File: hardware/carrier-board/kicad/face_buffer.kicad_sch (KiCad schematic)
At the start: 0 parts

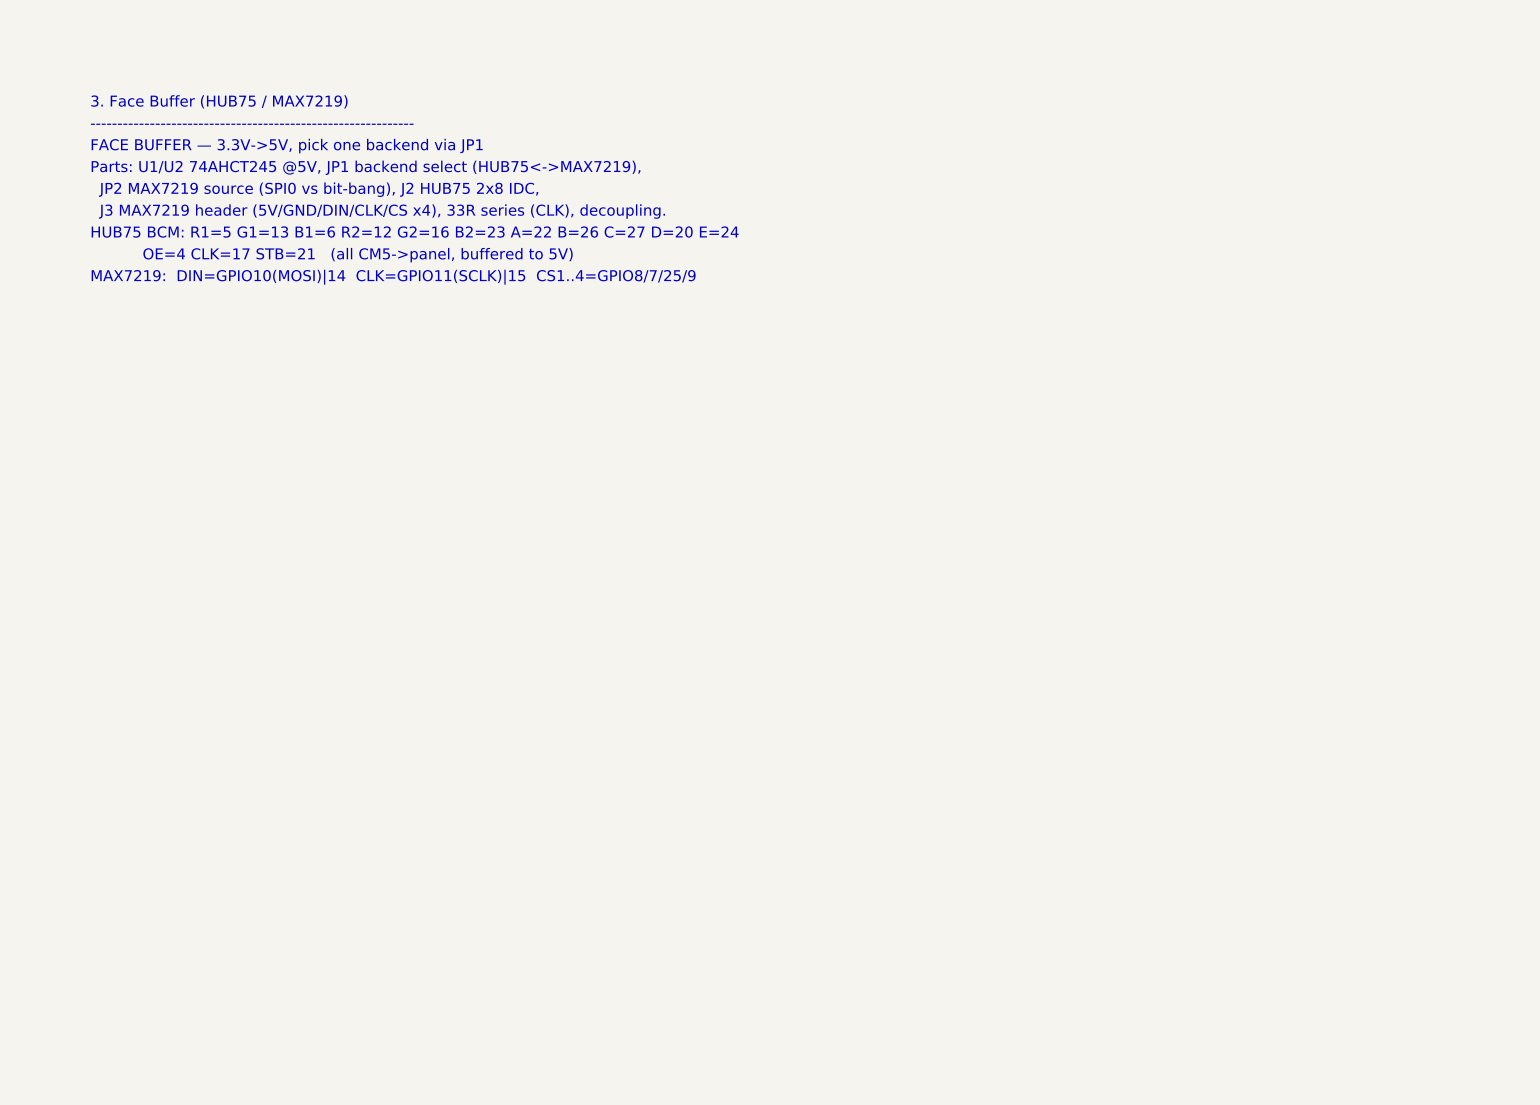
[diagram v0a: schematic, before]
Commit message: Carrier KiCad: populate face_buffer proof sheet (HUB75/MAX7219 '245 buffer)
Turn the face_buffer stub into a real, openable schematic as a format proof
before populating the remaining sheets:

- U1/U2 74AHCT245 @5V, DIR=+5V /OE=GND; R1-R3 33R series on CLK/LAT/OE;
  J2 HUB75 2x8 IDC, J3 MAX7219 1x8 header, JP2 DIN source select, C1/C2 decoupling.
- Netlist via labels placed on pin connection points (survives Update-from-Library):
  CM5-side GPIOxx as hierarchical labels per PINMAP kHub75 map, buffered
  R1/G1/.../E to J2, +5V/GND as global labels.
- KiCad 9 format (20250114), official lib_ids with embedded cached bodies.

Generated by populate_face_buffer.py (to be folded into generate_skeleton.py
once the format is validated in KiCad).
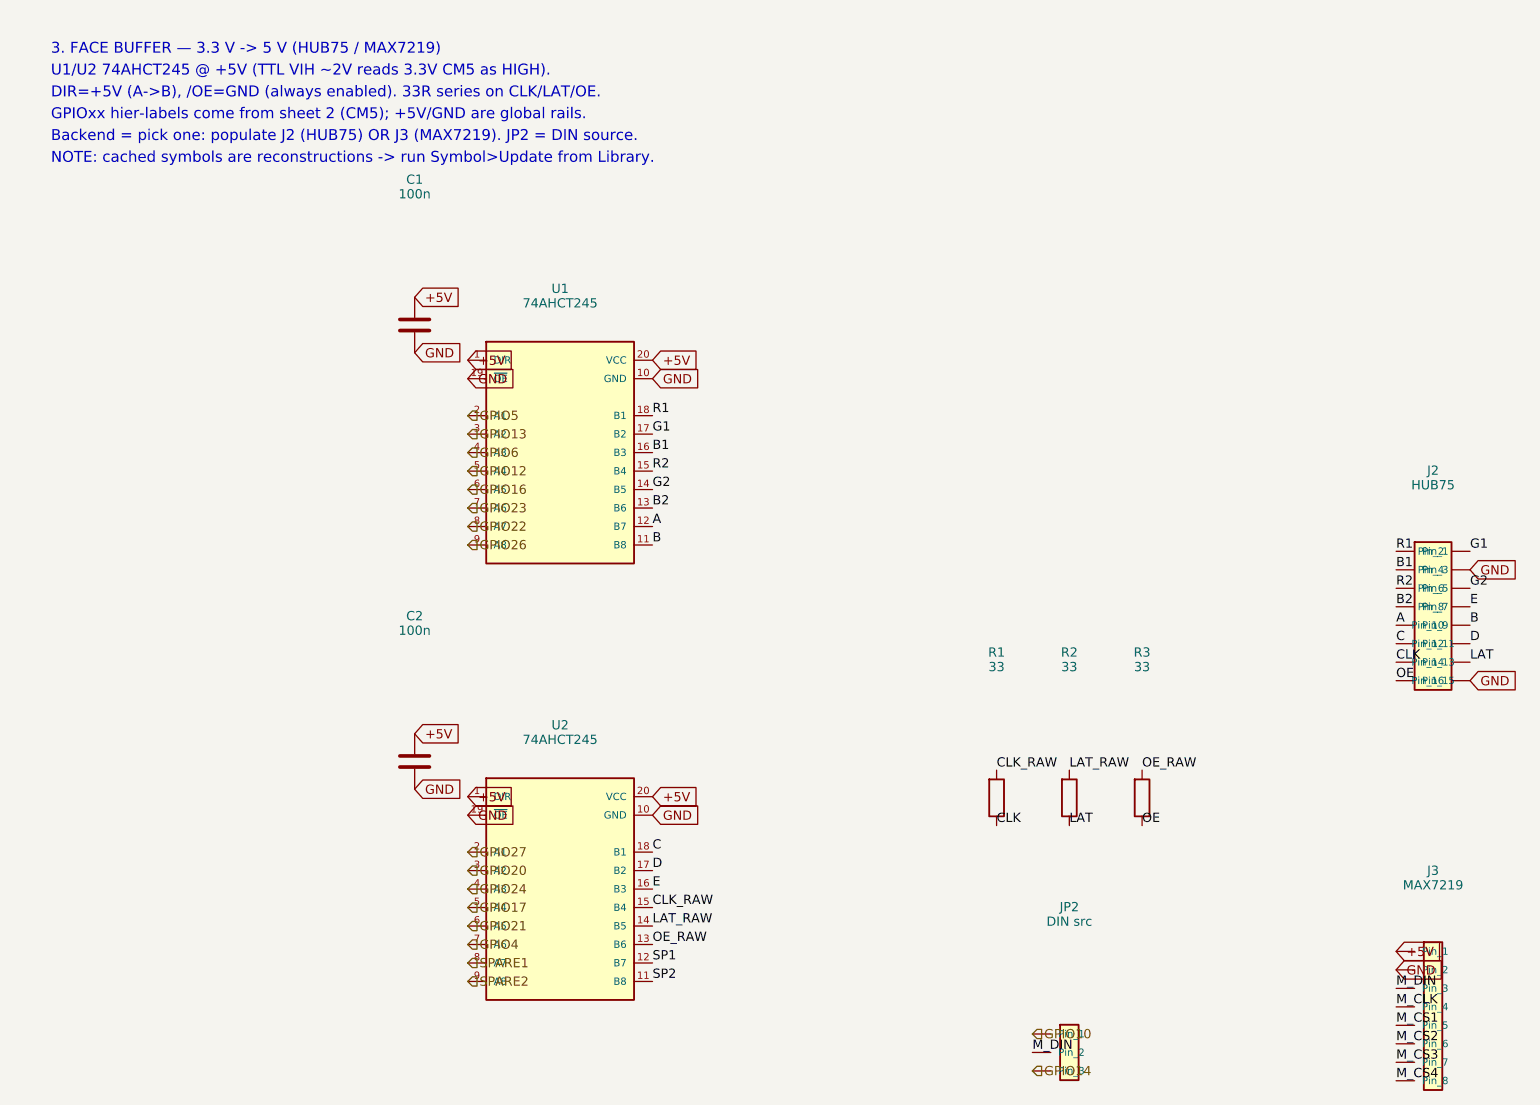
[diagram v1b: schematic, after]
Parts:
- added C1, C2: 100n, symbol Device:C
- added J2: HUB75, symbol Connector_Generic:Conn_02x08_Odd_Even
- added J3: MAX7219, symbol Connector_Generic:Conn_01x08
- added JP2: DIN src, symbol Connector_Generic:Conn_01x03
- added R1, R2, R3: 33, symbol Device:R
- added U1, U2: 74AHCT245, symbol 74xx:74AHCT245
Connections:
- new net +5V: C1.1, C2.1, J3.1 (Pin_1), U1.1 (DIR), U1.20 (VCC), U2.1 (DIR), U2.20 (VCC)
- new net A: J2.9 (Pin_9), U1.12 (B7)
- new net B: J2.10 (Pin_10), U1.11 (B8)
- new net B1: J2.3 (Pin_3), U1.16 (B3)
- new net B2: J2.7 (Pin_7), U1.13 (B6)
- new net C: J2.11 (Pin_11), U2.18 (B1)
- new net CLK: J2.13 (Pin_13), R1.2
- new net CLK_RAW: R1.1, U2.15 (B4)
- new net D: J2.12 (Pin_12), U2.17 (B2)
- new net E: J2.8 (Pin_8), U2.16 (B3)
- new net G1: J2.2 (Pin_2), U1.17 (B2)
- new net G2: J2.6 (Pin_6), U1.14 (B5)
- new net GND: C1.2, C2.2, J2.16 (Pin_16), J2.4 (Pin_4), J3.2 (Pin_2), U1.10 (GND), U1.19 (~{OE}), U2.10 (GND), U2.19 (~{OE})
- new net GPIO10: JP2.1 (Pin_1)
- new net GPIO12: U1.5 (A4)
- new net GPIO13: U1.3 (A2)
- new net GPIO14: JP2.3 (Pin_3)
- new net GPIO16: U1.6 (A5)
- new net GPIO17: U2.5 (A4)
- new net GPIO20: U2.3 (A2)
- new net GPIO21: U2.6 (A5)
- new net GPIO22: U1.8 (A7)
- new net GPIO23: U1.7 (A6)
- new net GPIO24: U2.4 (A3)
- new net GPIO26: U1.9 (A8)
- new net GPIO27: U2.2 (A1)
- new net GPIO4: U2.7 (A6)
- new net GPIO5: U1.2 (A1)
- new net GPIO6: U1.4 (A3)
- new net LAT: J2.14 (Pin_14), R2.2
- new net LAT_RAW: R2.1, U2.14 (B5)
- new net M_CLK: J3.4 (Pin_4)
- new net M_CS1: J3.5 (Pin_5)
- new net M_CS2: J3.6 (Pin_6)
- new net M_CS3: J3.7 (Pin_7)
- new net M_CS4: J3.8 (Pin_8)
- new net M_DIN: J3.3 (Pin_3), JP2.2 (Pin_2)
- new net OE: J2.15 (Pin_15), R3.2
- new net OE_RAW: R3.1, U2.13 (B6)
- new net R1: J2.1 (Pin_1), U1.18 (B1)
- new net R2: J2.5 (Pin_5), U1.15 (B4)
- new net SP1: U2.12 (B7)
- new net SP2: U2.11 (B8)
- new net SPARE1: U2.8 (A7)
- new net SPARE2: U2.9 (A8)
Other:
- note added: "3. FACE BUFFER — 3.3 V -> 5 V (HUB75 / MAX7219)"
- note added: "Backend = pick one: populate J2 (HUB75) OR J3 (MAX7219). JP2 = DIN source."
- note added: "DIR=+5V (A->B), /OE=GND (always enabled). 33R series on CLK/LAT/OE."
- note added: "GPIOxx hier-labels come from sheet 2 (CM5); +5V/GND are global rails."
- note added: "NOTE: cached symbols are reconstructions -> run Symbol>Update from Library."
- note added: "U1/U2 74AHCT245 @ +5V (TTL VIH ~2V reads 3.3V CM5 as HIGH)."
- note removed: "------------------------------------------------------------"
- note removed: "3. Face Buffer (HUB75 / MAX7219)"
- note removed: "FACE BUFFER — 3.3V->5V, pick one backend via JP1"
- note removed: "HUB75 BCM: R1=5 G1=13 B1=6 R2=12 G2=16 B2=23 A=22 B=26 C=27 D=20 E=24"
- note removed: "J3 MAX7219 header (5V/GND/DIN/CLK/CS x4), 33R series (CLK), decoupling."
- note removed: "JP2 MAX7219 source (SPI0 vs bit-bang), J2 HUB75 2x8 IDC,"
- note removed: "MAX7219: DIN=GPIO10(MOSI)|14 CLK=GPIO11(SCLK)|15 CS1..4=GPIO8/7/25/9"
- note removed: "OE=4 CLK=17 STB=21 (all CM5->panel, buffered to 5V)"
- note removed: "Parts: U1/U2 74AHCT245 @5V, JP1 backend select (HUB75<->MAX7219),"

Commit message: Carrier KiCad: make face_buffer HUB75-only (RP2354B owns other I/O)
Architecture pivot: CM5 drives only HUB75; a dedicated RP2354B I/O coprocessor
owns WS2812, I2C sensors, buttons/boop, MAX7219, and servos (USB-CDC to CM5).
So the CM5-side face buffer is HUB75-only -- drop J3 MAX7219 header + JP2 source
select from this sheet (they move to the RP2354B sheets).
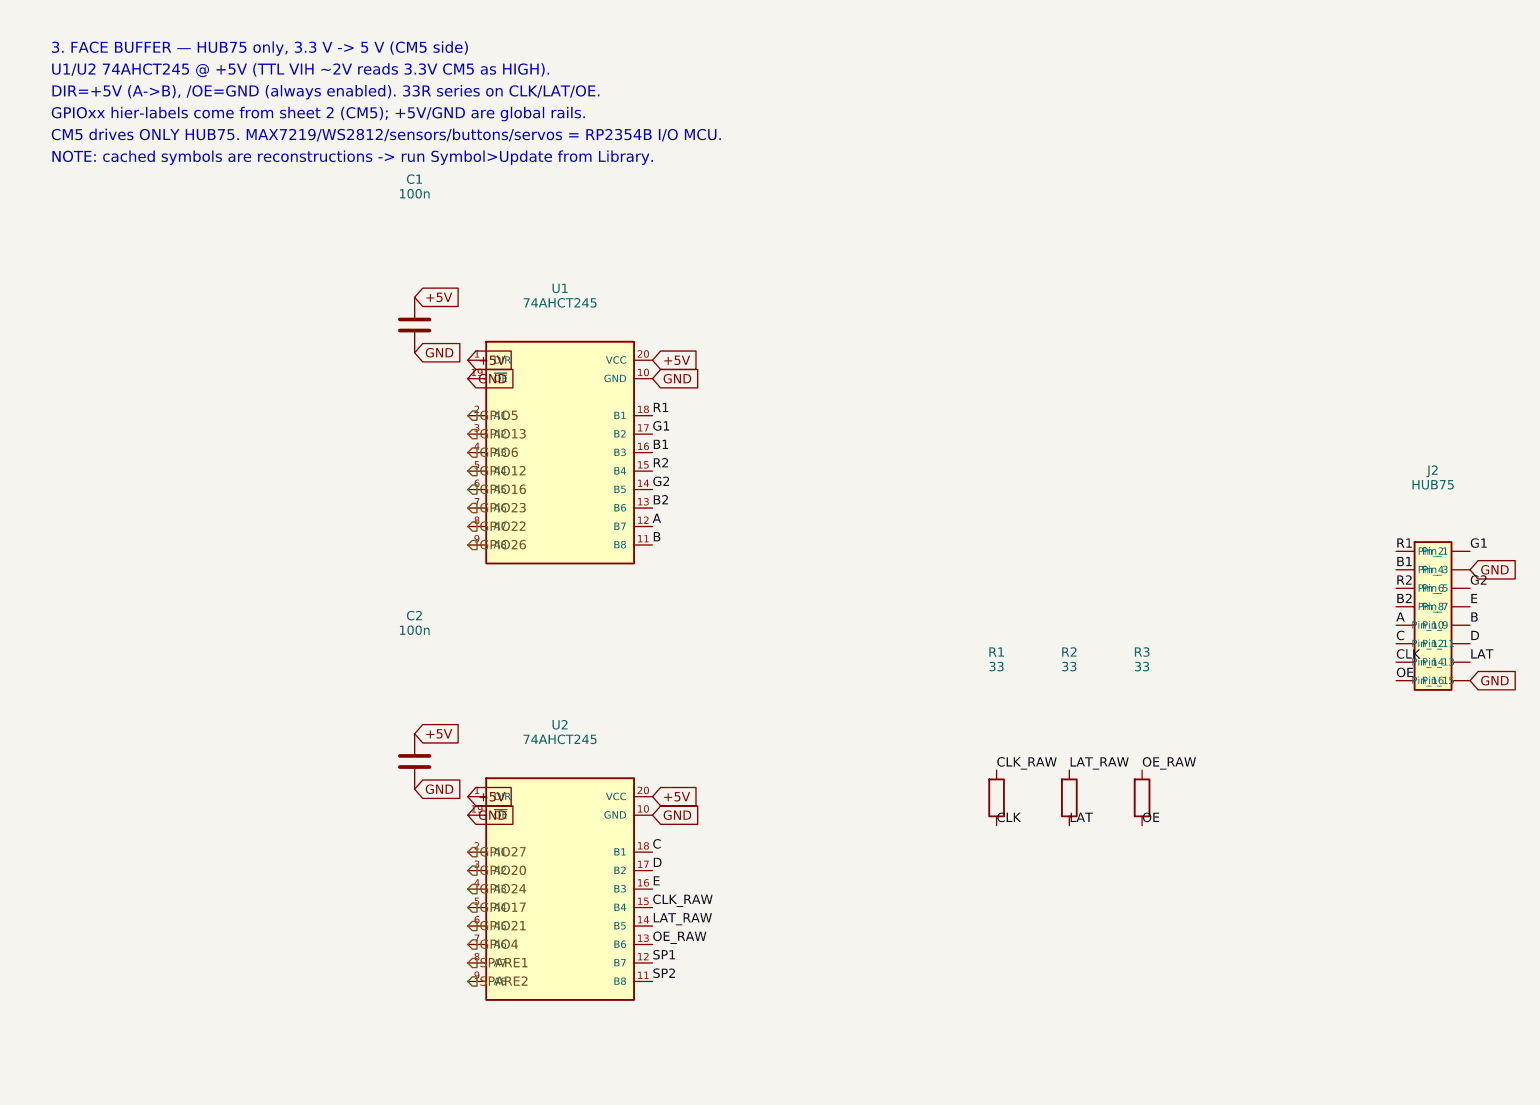
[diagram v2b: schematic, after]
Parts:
- removed J3: MAX7219, symbol Connector_Generic:Conn_01x08
- removed JP2: DIN src, symbol Connector_Generic:Conn_01x03
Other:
- note added: "3. FACE BUFFER — HUB75 only, 3.3 V -> 5 V (CM5 side)"
- note added: "CM5 drives ONLY HUB75. MAX7219/WS2812/sensors/buttons/servos = RP2354B I/O MCU."
- note removed: "3. FACE BUFFER — 3.3 V -> 5 V (HUB75 / MAX7219)"
- note removed: "Backend = pick one: populate J2 (HUB75) OR J3 (MAX7219). JP2 = DIN source."
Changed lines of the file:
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@@
     (company "ProtoHUD")
   )
-  (text "3. FACE BUFFER — 3.3 V -> 5 V (HUB75 / MAX7219)" (at 20 18.0 0) (effects (font (size 1.5 1.5)) (justify left bottom)))
+  (text "3. FACE BUFFER — HUB75 only, 3.3 V -> 5 V (CM5 side)" (at 20 18.0 0) (effects (font (size 1.5 1.5)) (justify left bottom)))
   (text "U1/U2 74AHCT245 @ +5V (TTL VIH ~2V reads 3.3V CM5 as HIGH)." (at 20 21.0 0) (effects (font (size 1.5 1.5)) (justify left bottom)))
   (text "DIR=+5V (A->B), /OE=GND (always enabled). 33R series on CLK/LAT/OE." (at 20 24.0 0) (effects (font (size 1.5 1.5)) (justify left bottom)))
   (text "GPIOxx hier-labels come from sheet 2 (CM5); +5V/GND are global rails." (at 20 27.0 0) (effects (font (size 1.5 1.5)) (justify left bottom)))
-  (text "Backend = pick one: populate J2 (HUB75) OR J3 (MAX7219). JP2 = DIN source." (at 20 30.0 0) (effects (font (size 1.5 1.5)) (justify left bottom)))
+  (text "CM5 drives ONLY HUB75. MAX7219/WS2812/sensors/buttons/servos = RP2354B I/O MCU." (at 20 30.0 0) (effects (font (size 1.5 1.5)) (justify left bottom)))
   (text "NOTE: cached symbols are reconstructions -> run Symbol>Update from Library." (at 20 33.0 0) (effects (font (size 1.5 1.5)) (justify left bottom)))
   (symbol
@@
         (path "/eff6a452-77ae-416d-87a8-cfe219f371e8"
           (reference "J2") (unit 1))))
-  )
-  (symbol
-    (lib_id "Connector_Generic:Conn_01x08")
-    (at 210.00 150.00 0)
-    (unit 1)
-    (exclude_from_sim no) (in_bom yes) (on_board yes) (dnp no)
-    (property "Reference" "J3" (at 210.00 130.00 0) (effects (font (size 1.27 1.27))))
-    (property "Value" "MAX7219" (at 210.00 132.00 0) (effects (font (size 1.27 1.27))))
-    (property "Footprint" "" (at 210.00 150.00 0) (effects (font (size 1.27 1.27)) (hide yes)))
-    (property "Datasheet" "" (at 210.00 150.00 0) (effects (font (size 1.27 1.27)) (hide yes)))
-    (pin "1")
-    (pin "2")
-    (pin "3")
-    (pin "4")
-    (pin "5")
-    (pin "6")
-    (pin "7")
-    (pin "8")
-    (instances
-      (project "ProtoHUD-Carrier"
-        (path "/eff6a452-77ae-416d-87a8-cfe219f371e8"
-          (reference "J3") (unit 1))))
-  )
-  (symbol
-    (lib_id "Connector_Generic:Conn_01x03")
-    (at 160.00 155.00 0)
-    (unit 1)
-    (exclude_from_sim no) (in_bom yes) (on_board yes) (dnp no)
-    (property "Reference" "JP2" (at 160.00 135.00 0) (effects (font (size 1.27 1.27))))
-    (property "Value" "DIN src" (at 160.00 137.00 0) (effects (font (size 1.27 1.27))))
-    (property "Footprint" "" (at 160.00 155.00 0) (effects (font (size 1.27 1.27)) (hide yes)))
-    (property "Datasheet" "" (at 160.00 155.00 0) (effects (font (size 1.27 1.27)) (hide yes)))
-    (pin "1")
-    (pin "2")
-    (pin "3")
-    (instances
-      (project "ProtoHUD-Carrier"
-        (path "/eff6a452-77ae-416d-87a8-cfe219f371e8"
-          (reference "JP2") (unit 1))))
   )
   (symbol
@@
   (label "OE" (at 204.92 103.89 180) (effects (font (size 1.27 1.27)) (justify left bottom)))
   (global_label "GND" (shape input) (at 215.08 103.89 0) (effects (font (size 1.27 1.27)) (justify left)))
-  (global_label "+5V" (shape input) (at 204.92 141.11 180) (effects (font (size 1.27 1.27)) (justify left)))
-  (global_label "GND" (shape input) (at 204.92 143.65 180) (effects (font (size 1.27 1.27)) (justify left)))
-  (label "M_DIN" (at 204.92 146.19 180) (effects (font (size 1.27 1.27)) (justify left bottom)))
-  (label "M_CLK" (at 204.92 148.73 180) (effects (font (size 1.27 1.27)) (justify left bottom)))
-  (label "M_CS1" (at 204.92 151.27 180) (effects (font (size 1.27 1.27)) (justify left bottom)))
-  (label "M_CS2" (at 204.92 153.81 180) (effects (font (size 1.27 1.27)) (justify left bottom)))
-  (label "M_CS3" (at 204.92 156.35 180) (effects (font (size 1.27 1.27)) (justify left bottom)))
-  (label "M_CS4" (at 204.92 158.89 180) (effects (font (size 1.27 1.27)) (justify left bottom)))
-  (hierarchical_label "GPIO10" (shape input) (at 154.92 152.46 180) (effects (font (size 1.27 1.27)) (justify left)))
-  (label "M_DIN" (at 154.92 155.00 180) (effects (font (size 1.27 1.27)) (justify left bottom)))
-  (hierarchical_label "GPIO14" (shape input) (at 154.92 157.54 180) (effects (font (size 1.27 1.27)) (justify left)))
   (global_label "+5V" (shape input) (at 70.00 51.19 0) (effects (font (size 1.27 1.27)) (justify left)))
   (global_label "GND" (shape input) (at 70.00 58.81 0) (effects (font (size 1.27 1.27)) (justify left)))

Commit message: Carrier docs + KiCad plan: full two-brain pass (CM5 HUB75 + RP2354B I/O)
Propagate the two-brain architecture across the whole doc set and KiCad plan:
- REQUIREMENTS: restructured M1-M12 (CM5 HUB75; RP2354B core/MAX7219/WS2812/
  sensors/buttons/servos; USB selector + standalone program port); N-list reworked.
- POWER: add +V_SERVO and +3V3_RP rails, servo current budget, updated worked
  total + protection; sensors now on +3V3_RP not CM5 3V3.
- CONNECTORS: J3 re-sourced to RP2354B SPI0, J4 4 WS2812 zones, J5 +SENS_INT,
  J6 BTN1..10, add J12 USB-C, J20-J27 servos, SW1 USB selector, SWD/UART hdrs;
  drop JP1/JP2; fans presented as RP2354B-default-or-CM5 (decision flagged).
- BOM: add RP2354B core, '125/'245 (RP side), USB mux/USB-C/ESD, servo headers,
  +3V3_RP reg; fix '125 double-count and stale HUB75/MAX7219-shared-buffer/JP1.
- MULTI-BACKEND: HUB75+MAX7219 now simultaneous (different brains); firmware
  CompositePanelOutput is the sole remaining blocker.
- IO-EXPANSION: RP2354B is the primary I/O backbone; I2C expanders secondary.
- kicad: 11-sheet plan, stable UUIDs, generator skips populated face_buffer.
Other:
- title: ProtoHUD Carrier — 3. Face Buffer (HUB75 / MAX7219) -> ProtoHUD Carrier — 3. Face Buffer (HUB75)
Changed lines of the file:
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@@
   (paper "A3")
   (title_block
-    (title "ProtoHUD Carrier — 3. Face Buffer (HUB75 / MAX7219)")
+    (title "ProtoHUD Carrier — 3. Face Buffer (HUB75)")
     (rev "A")
     (company "ProtoHUD")
